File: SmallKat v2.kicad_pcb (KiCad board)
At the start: 2 copper layers, 89 x 99 mm, 187 parts, among them IC1 TPS562201DDCR, IC2 TPS40192DRCT, J1 Conn_01x03_Male, J10 Conn_01x03_Male, J11 Conn_01x03_Male, J12 Conn_01x03_Male, J13 Conn_01x03_Male, J14 Conn_01x03_Male, J15 Conn_01x03_Male, J16 Conn_01x03_Male, J17 Conn_01x03_Male, J18 Conn_01x02_Male, J19 USB_C_Receptacle, J2 Conn_01x03_Male, J20 USB_C_Receptacle, J3 Conn_01x03_Male, J4 Conn_01x03_Male, J5 Conn_01x03_Male, J6 Conn_01x03_Male, J7 Conn_01x03_Male, J8 Conn_01x03_Male, J9 Conn_01x02_Male, Q1 BUK9M120-100EX, Q2 BUK9M120-100EX, Q3 MMBT3904, Q4 MMBT3904, Q5 MMBT3904, Q6 MMBT3904, Q7 2N3905, SW1 SW_SPST, SW2 SW_SPST, SW3 SW_SPST, SW4 SW_SPST, U1 BNO055, U2 MIC5365-3.3YC5, U3 ESP32-WROOM-32, U4 CP2102N-A01-GQFN24, U5 MCP73831-2-OT, U6 MIC5365-3.3YC5, U7 ESP32-WROOM-32, U8 CP2102N-A01-GQFN24, U9 WIICHUCK, Y1 32.768kHz

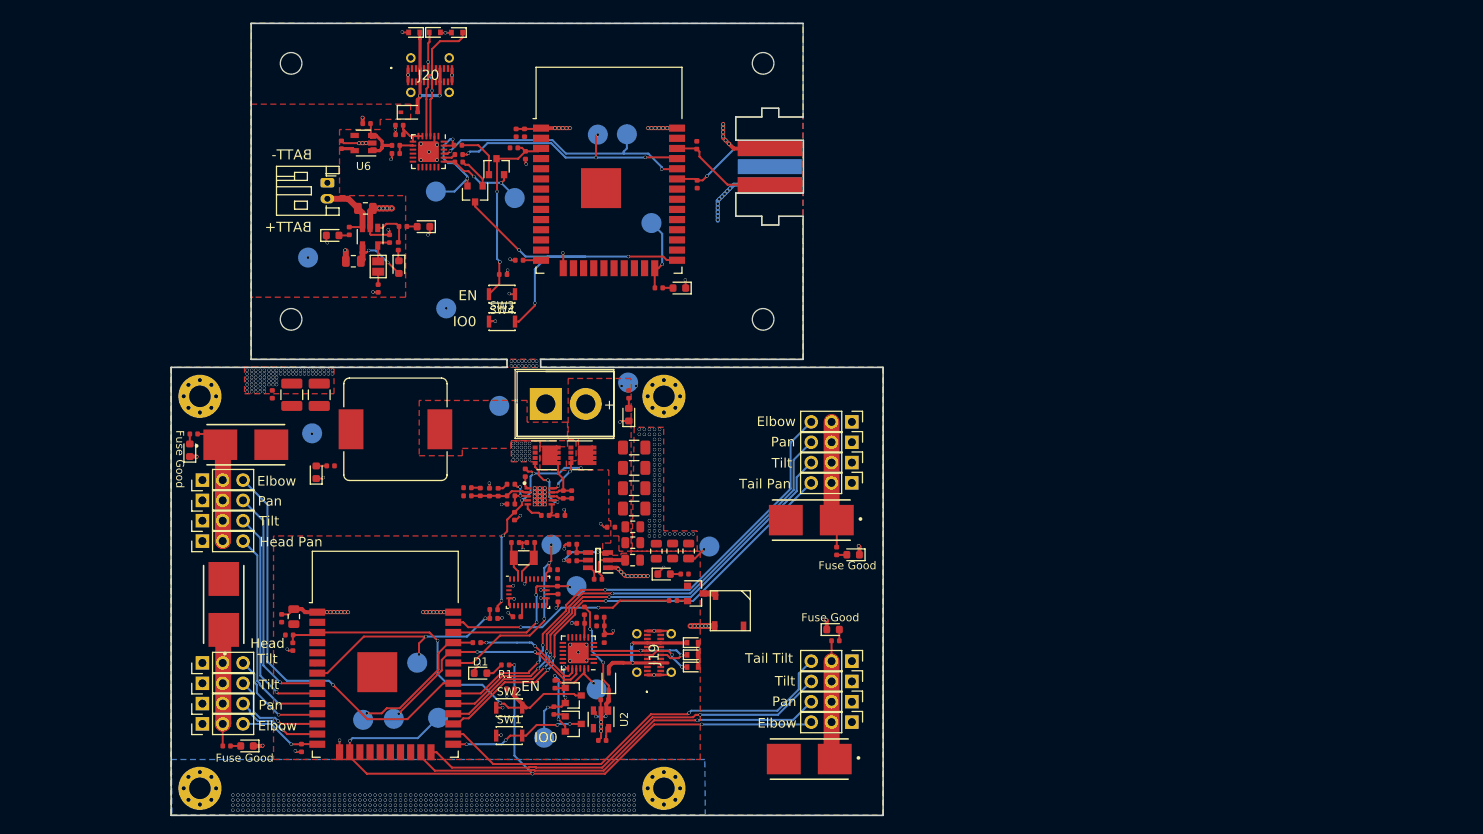
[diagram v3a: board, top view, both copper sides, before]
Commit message: In progress of charging implimentation
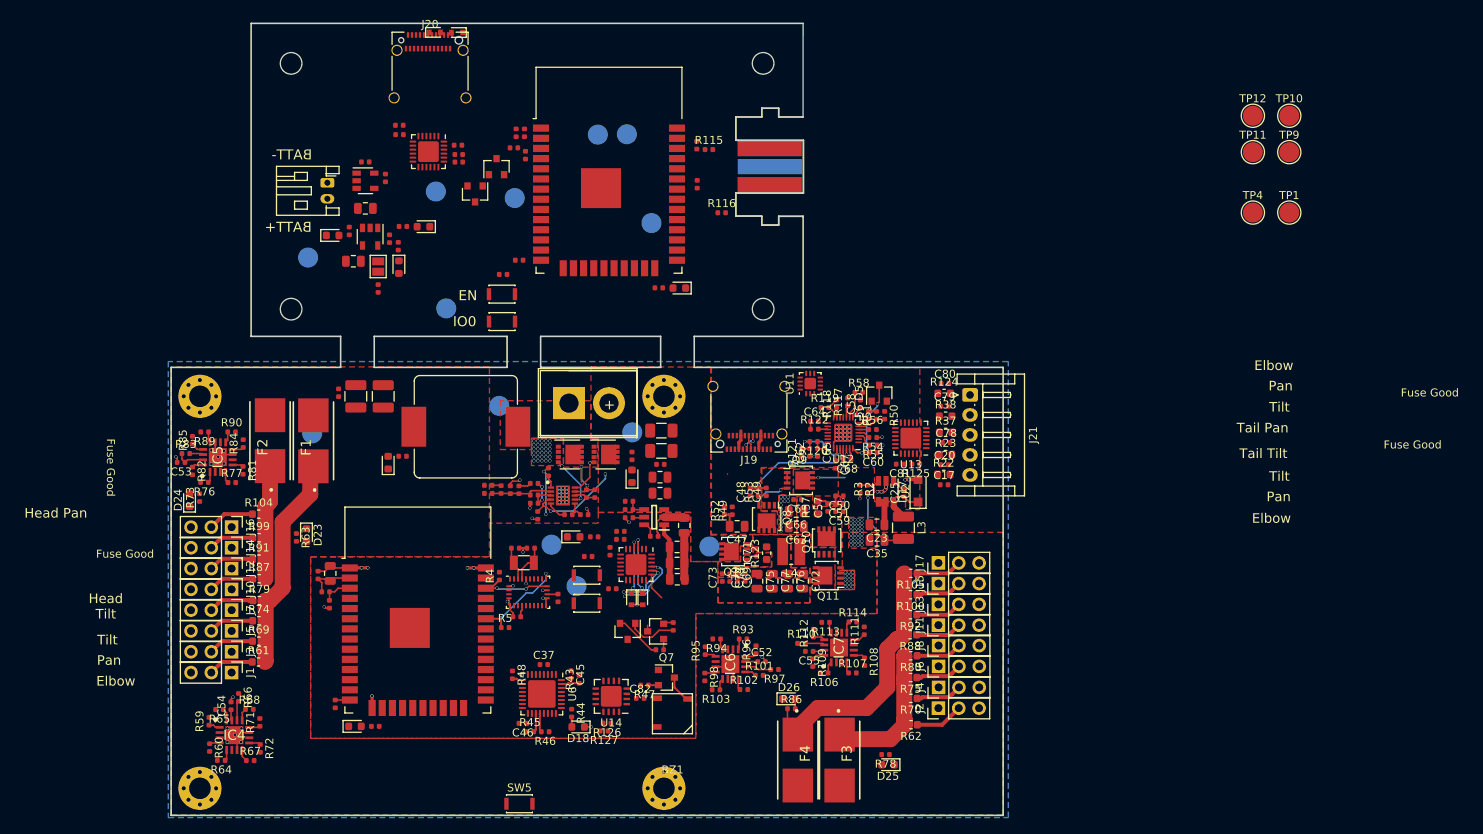
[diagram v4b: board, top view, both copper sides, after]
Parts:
- removed D13: D_TVS, Diode_SMD:D_SOD-523
- removed D14, D6: D_Schottky, Diode_SMD:D_SOD-323
- removed D19, D20: LED, LED_SMD:LED_0603_1608Metric
- added C30: 1uF, Capacitor_SMD:C_0402_1005Metric, F.Cu at (123.2, 61.2)
- added C42: 1uF, Capacitor_SMD:C_0402_1005Metric, F.Cu at (125.8, 63.2)
- added C45: 0.1uF, Capacitor_SMD:C_0402_1005Metric, F.Cu at (148.9, 125.3)
- added C46: 0.1uF, Capacitor_SMD:C_0402_1005Metric, F.Cu at (142.9, 131.4)
- added C47: 2.2uF, Capacitor_SMD:C_0805_2012Metric, F.Cu at (169.7, 106.8)
- added C48: 2200pF, Capacitor_SMD:C_0402_1005Metric, F.Cu at (171.3, 102.5)
- added C49: 0.1uF, Capacitor_SMD:C_0402_1005Metric, F.Cu at (173.3, 102.4)
- added C50: 1uF, Capacitor_SMD:C_0402_1005Metric, F.Cu at (182.5, 103.0)
- added C51: 0.1uF, Capacitor_SMD:C_0402_1005Metric, F.Cu at (182.5, 104.0)
- added C52: 0.1uF, Capacitor_SMD:C_0402_1005Metric, F.Cu at (172.8, 123.7)
- added C53: 0.1uF, Capacitor_SMD:C_0402_1005Metric, F.Cu at (100.2, 98.8)
- added C54: 0.1uF, Capacitor_SMD:C_0402_1005Metric, F.Cu at (106.5, 129.2)
- added C55: 0.1uF, Capacitor_SMD:C_0402_1005Metric, F.Cu at (178.7, 122.4)
- added C56: 100pF, Capacitor_SMD:C_0402_1005Metric, F.Cu at (186.1, 92.8)
- added C57: 0.1uF, Capacitor_SMD:C_0402_1005Metric, F.Cu at (181.1, 104.4)
- added C58: 100pF, Capacitor_SMD:C_0402_1005Metric, F.Cu at (185.1, 91.5)
- added C59: 0.1uF, Capacitor_SMD:C_0402_1005Metric, F.Cu at (182.5, 104.9)
- added C60: 1uF, Capacitor_SMD:C_0402_1005Metric, F.Cu at (186.7, 97.5)
- added C61: 1uF, Capacitor_SMD:C_0402_1005Metric, F.Cu at (177.2, 103.4)
- added C62: 0.01uF, Capacitor_SMD:C_0402_1005Metric, F.Cu at (178.8, 97.5)
- added C63: 10uF, Capacitor_SMD:C_0805_2012Metric, F.Cu at (177.1, 106.8)
- added C64: 0.1uF, Capacitor_SMD:C_0402_1005Metric, F.Cu at (179.4, 93.6)
- added C65: 1uF, Capacitor_SMD:C_0402_1005Metric, F.Cu at (179.8, 97.5)
- added C66: 10uF, Capacitor_SMD:C_0805_2012Metric, F.Cu at (177.1, 104.9)
- added C67: 470pF, Capacitor_SMD:C_0402_1005Metric, F.Cu at (182.0, 99.0)
- added C68: 0.047uF, Capacitor_SMD:C_0402_1005Metric, F.Cu at (183.5, 98.4)
- added C69: 10uF, Capacitor_SMD:C_0402_1005Metric, F.Cu at (169.8, 113.2)
- added C70: 0.1uF, Capacitor_SMD:C_0402_1005Metric, F.Cu at (170.7, 113.1)
- added C71: 0.1uF, Capacitor_SMD:C_0402_1005Metric, F.Cu at (172.2, 110.0)
- added C72: 22uF, Capacitor_SMD:C_0805_2012Metric, F.Cu at (177.9, 113.6)
- added C73: 0.1uF, Capacitor_SMD:C_0402_1005Metric, F.Cu at (167.8, 113.2)
- added C74: 10uF, Capacitor_SMD:C_0402_1005Metric, F.Cu at (168.8, 113.2)
- added C75: 22uF, Capacitor_SMD:C_0805_2012Metric, F.Cu at (172.2, 113.6)
- added C76: 22uF, Capacitor_SMD:C_0805_2012Metric, F.Cu at (176.0, 113.6)
- added C77: 22uF, Capacitor_SMD:C_0805_2012Metric, F.Cu at (174.1, 113.6)
- added C78: 0.1uF, Capacitor_SMD:C_0402_1005Metric, F.Cu at (195.8, 96.3)
- added C79: 0.1uF, Capacitor_SMD:C_0402_1005Metric, F.Cu at (195.7, 91.7)
- added C80: 0.1uF, Capacitor_SMD:C_0402_1005Metric, F.Cu at (195.7, 88.9)
- added C81: 1uF, Capacitor_SMD:C_0402_1005Metric, F.Cu at (190.1, 99.0)
- added C82: 1uF, Capacitor_SMD:C_0402_1005Metric, F.Cu at (157.6, 128.2)
- added D23: LED, LED_SMD:LED_0603_1608Metric, F.Cu at (115.9, 107.8)
- added D24: LED, LED_SMD:LED_0603_1608Metric, F.Cu at (101.3, 103.5)
- added D25: LED, LED_SMD:LED_0603_1608Metric, F.Cu at (188.6, 136.5)
- added D26: LED, LED_SMD:LED_0603_1608Metric, F.Cu at (176.2, 128.3)
- added IC4: MAX34409ETE+, MAX34409ETE+:QFN65P400X400X80-17N, F.Cu at (106.9, 132.8)
- added IC5: MAX34409ETE+, MAX34409ETE+:QFN65P400X400X80-17N, F.Cu at (104.8, 98.1)
- added IC6: MAX34409ETE+, MAX34409ETE+:QFN65P400X400X80-17N, F.Cu at (168.9, 124.0)
- added IC7: MAX34409ETE+, MAX34409ETE+:QFN65P400X400X80-17N, F.Cu at (182.4, 121.9)
- added J21: Conn_01x05_Male, Connector_JST:JST_EH_S5B-EH_1x05_P2.50mm_Horizontal, F.Cu at (198.8, 90.3)
- added L3: 15uH, Inductor_SMD:L_1210_3225Metric, F.Cu at (190.5, 106.9)
- added L4: L, Inductor_SMD:L_Wuerth_MAPI-3020, F.Cu at (176.5, 109.9)
- added Q10: CSD17307Q5A, Package_TO_SOT_SMD:LFPAK33, F.Cu at (180.9, 108.7)
- added Q11: CSD17307Q5A, Package_TO_SOT_SMD:LFPAK33, F.Cu at (181.1, 112.9)
- added Q12: Si7141DP, Package_TO_SOT_SMD:LFPAK33, F.Cu at (169.4, 109.9)
- added Q8: BUK9M120-100EX, Package_TO_SOT_SMD:LFPAK33, F.Cu at (173.4, 105.7)
- added Q9: BUK9M120-100EX, Package_TO_SOT_SMD:LFPAK33, F.Cu at (177.5, 101.0)
- added R100: 0.01R, Resistor_SMD:R_0603_1608Metric, F.Cu at (191.4, 115.3)
- added R101: 100R, Resistor_SMD:R_0402_1005Metric, F.Cu at (172.5, 125.4)
- added R102: 100R, Resistor_SMD:R_0402_1005Metric, F.Cu at (170.6, 127.2)
- added R103: 100R, Resistor_SMD:R_0402_1005Metric, F.Cu at (167.1, 127.2)
- added R104: 0.01R, Resistor_SMD:R_0603_1608Metric, F.Cu at (109.9, 105.2)
- added R105: 0.01R, Resistor_SMD:R_0603_1608Metric, F.Cu at (191.4, 112.6)
- added R106: 100R, Resistor_SMD:R_0402_1005Metric, F.Cu at (180.6, 125.1)
- added R107: 100R, Resistor_SMD:R_0402_1005Metric, F.Cu at (184.1, 125.1)
- added R108: 100R, Resistor_SMD:R_0402_1005Metric, F.Cu at (185.7, 123.7)
- added R109: 100R, Resistor_SMD:R_0402_1005Metric, F.Cu at (179.2, 123.8)
- added R110: 0R, Resistor_SMD:R_0402_1005Metric, F.Cu at (177.8, 121.4)
- added R111: 100R, Resistor_SMD:R_0402_1005Metric, F.Cu at (185.6, 119.8)
- added R112: 100R, Resistor_SMD:R_0402_1005Metric, F.Cu at (179.2, 120.1)
- added R113: 100R, Resistor_SMD:R_0402_1005Metric, F.Cu at (180.8, 118.8)
- added R114: 100R, Resistor_SMD:R_0402_1005Metric, F.Cu at (184.2, 118.7)
- added R115: 10K, Resistor_SMD:R_0402_1005Metric, F.Cu at (166.2, 59.6)
- added R116: 10K, Resistor_SMD:R_0402_1005Metric, F.Cu at (167.8, 67.5)
- added R117: 10K, Resistor_SMD:R_0402_1005Metric, F.Cu at (183.5, 91.2)
- added R118: 3M, Resistor_SMD:R_0402_1005Metric, F.Cu at (182.1, 91.5)
- added R119: 10K, Resistor_SMD:R_0402_1005Metric, F.Cu at (180.7, 91.9)
- added R120: 316K, Resistor_SMD:R_0402_1005Metric, F.Cu at (179.3, 96.2)
- added R121: 100K, Resistor_SMD:R_0402_1005Metric, F.Cu at (177.8, 97.5)
- added R122: 10R, Resistor_SMD:R_0402_1005Metric, F.Cu at (179.4, 94.6)
- added R123: 0.01R, Resistor_SMD:R_0603_1608Metric, F.Cu at (173.4, 110.1)
- added R124: 47R, Resistor_SMD:R_0603_1608Metric, F.Cu at (195.6, 90.1)
- added R125: 10K, Resistor_SMD:R_0402_1005Metric, F.Cu at (192.1, 99.0)
- added R126: 10K, Resistor_SMD:R_0402_1005Metric, F.Cu at (153.4, 131.3)
- added R127: 10K, Resistor_SMD:R_0402_1005Metric, F.Cu at (153.1, 132.3)
- added R48: 10K, Resistor_SMD:R_0402_1005Metric, F.Cu at (141.6, 125.3)
- added R49: 3.9K, Resistor_SMD:R_0402_1005Metric, F.Cu at (169.1, 104.8)
- added R50: 430K, Resistor_SMD:R_0402_1005Metric, F.Cu at (188.2, 92.9)
- added R51: 66.5K, Resistor_SMD:R_0402_1005Metric, F.Cu at (187.1, 92.9)
- added R52: 3.9K, Resistor_SMD:R_0402_1005Metric, F.Cu at (168.2, 104.8)
- added R53: 4.7R, Resistor_SMD:R_0402_1005Metric, F.Cu at (172.3, 102.5)
- added R54: 4.02K, Resistor_SMD:R_0402_1005Metric, F.Cu at (186.7, 95.7)
- added R55: 4.02K, Resistor_SMD:R_0402_1005Metric, F.Cu at (186.7, 96.6)
- added R56: 10K, Resistor_SMD:R_0402_1005Metric, F.Cu at (186.6, 94.7)
- added R57: 0.01R, Resistor_SMD:R_0603_1608Metric, F.Cu at (179.8, 104.4)
- added R58: 30.1K, Resistor_SMD:R_0402_1005Metric, F.Cu at (184.9, 90.0)
- added R59: 100R, Resistor_SMD:R_0402_1005Metric, F.Cu at (103.7, 131.1)
- added R60: 100R, Resistor_SMD:R_0402_1005Metric, F.Cu at (103.8, 134.4)
- added R61: 0.01R, Resistor_SMD:R_0603_1608Metric, F.Cu at (109.9, 123.7)
- added R62: 0.01R, Resistor_SMD:R_0603_1608Metric, F.Cu at (191.4, 131.6)
- added R63: 20K, Resistor_SMD:R_0402_1005Metric, F.Cu at (114.6, 108.1)
- added R64: 100R, Resistor_SMD:R_0402_1005Metric, F.Cu at (105.2, 136.0)
- added R65: 100R, Resistor_SMD:R_0402_1005Metric, F.Cu at (105.0, 129.7)
- added R66: 0R, Resistor_SMD:R_0402_1005Metric, F.Cu at (107.4, 128.1)
- added R67: 100R, Resistor_SMD:R_0402_1005Metric, F.Cu at (108.8, 136.0)
- added R68: 100R, Resistor_SMD:R_0402_1005Metric, F.Cu at (108.8, 129.6)
- added R69: 0.01R, Resistor_SMD:R_0603_1608Metric, F.Cu at (109.9, 121.1)
- added R70: 0.01R, Resistor_SMD:R_0603_1608Metric, F.Cu at (191.4, 128.2)
- added R71: 100R, Resistor_SMD:R_0402_1005Metric, F.Cu at (110.0, 131.2)
- added R72: 100R, Resistor_SMD:R_0402_1005Metric, F.Cu at (110.1, 134.5)
- added R73: 20K, Resistor_SMD:R_0402_1005Metric, F.Cu at (102.5, 103.2)
- added R74: 0.01R, Resistor_SMD:R_0603_1608Metric, F.Cu at (109.9, 118.5)
- added R75: 0.01R, Resistor_SMD:R_0603_1608Metric, F.Cu at (191.4, 125.7)
- added R76: 100R, Resistor_SMD:R_0402_1005Metric, F.Cu at (103.1, 101.2)
- added R77: 100R, Resistor_SMD:R_0402_1005Metric, F.Cu at (106.5, 101.3)
- added R78: 20K, Resistor_SMD:R_0402_1005Metric, F.Cu at (188.3, 135.3)
- added R79: 0.01R, Resistor_SMD:R_0603_1608Metric, F.Cu at (110.0, 116.0)
- added R80: 0.01R, Resistor_SMD:R_0603_1608Metric, F.Cu at (191.4, 122.9)
- added R81: 100R, Resistor_SMD:R_0402_1005Metric, F.Cu at (108.0, 99.8)
- added R82: 100R, Resistor_SMD:R_0402_1005Metric, F.Cu at (101.6, 99.8)
- added R83: 0R, Resistor_SMD:R_0402_1005Metric, F.Cu at (100.8, 97.7)
- added R84: 100R, Resistor_SMD:R_0402_1005Metric, F.Cu at (108.0, 96.4)
- added R85: 100R, Resistor_SMD:R_0402_1005Metric, F.Cu at (101.6, 96.0)
- added R86: 20K, Resistor_SMD:R_0402_1005Metric, F.Cu at (176.5, 129.6)
- added R87: 0.01R, Resistor_SMD:R_0603_1608Metric, F.Cu at (110.0, 113.3)
- added R88: 0.01R, Resistor_SMD:R_0603_1608Metric, F.Cu at (191.3, 120.3)
- added R89: 100R, Resistor_SMD:R_0402_1005Metric, F.Cu at (103.2, 95.0)
- added R90: 100R, Resistor_SMD:R_0402_1005Metric, F.Cu at (106.5, 95.0)
- added R91: 0.01R, Resistor_SMD:R_0603_1608Metric, F.Cu at (109.9, 110.8)
- added R92: 0.01R, Resistor_SMD:R_0603_1608Metric, F.Cu at (191.4, 117.8)
- added R93: 100R, Resistor_SMD:R_0402_1005Metric, F.Cu at (170.4, 120.8)
- added R94: 100R, Resistor_SMD:R_0402_1005Metric, F.Cu at (167.2, 120.8)
- added R95: 100R, Resistor_SMD:R_0402_1005Metric, F.Cu at (165.7, 122.3)
- added R96: 100R, Resistor_SMD:R_0402_1005Metric, F.Cu at (172.1, 122.2)
- added R97: 0R, Resistor_SMD:R_0402_1005Metric, F.Cu at (174.4, 124.7)
- added R98: 100R, Resistor_SMD:R_0402_1005Metric, F.Cu at (165.7, 125.6)
- added R99: 0.01R, Resistor_SMD:R_0603_1608Metric, F.Cu at (110.0, 108.2)
- added SW5: SW_SPST, Button_Switch_SMD:SW_SPST_CK_KXT3, F.Cu at (142.5, 141.4)
- added U10: MIC5365-3.3YC5, Package_TO_SOT_SMD:SOT-23-5, F.Cu at (123.3, 63.6)
- added U11: FUSB302BMPX, Package_DFN_QFN:WQFN-14-1EP_2.5x2.5mm_P0.5mm_EP1.45x1.45mm, F.Cu at (178.8, 88.9)
- added U12: BQ24770, Package_DFN_QFN:QFN-28-1EP_4x4mm_P0.4mm_EP2.3x2.3mm, F.Cu at (183.0, 95.0)
- added U13: bq76925, Package_DFN_QFN:QFN-24-1EP_4x4mm_P0.5mm_EP2.6x2.6mm, F.Cu at (191.4, 95.7)
- added U14: PCA9641, Package_DFN_QFN:UQFN-16-1EP_4x4mm_P0.65mm_EP2.6x2.6mm, F.Cu at (154.0, 128.0)
- C17, C20: value 47uF -> 0.1uF; footprint Capacitor_SMD:C_1206_3216Metric -> Capacitor_SMD:C_0402_1005Metric
- C23: value 1uF -> 2.2uF; footprint Capacitor_SMD:C_0402_1005Metric -> Capacitor_SMD:C_0805_2012Metric
- C25, C37: value 1uF -> 0.1uF
- C35: value 1uF -> 10uF; footprint Capacitor_SMD:C_0402_1005Metric -> Capacitor_SMD:C_0805_2012Metric
- D17: value LED -> MA2YD26; footprint LED_SMD:LED_0603_1608Metric -> Diode_SMD:D_SOD-123F
- D5: value D_TVS -> BAT54C; footprint Diode_SMD:D_SOD-523 -> Package_TO_SOT_SMD:SOT-23
- J19, J20: footprint U263-241N-4BQC11-1:U263241N4BQC111 -> Connector_USB:USB_C_Receptacle_Amphenol_12401610E4-2A_CircularHoles
- R1, R44: value R -> 330R
- R2: value 10K -> 1K
- R20: value 1K -> 20K
- R22, R37: value 10K -> 47R; footprint Resistor_SMD:R_0402_1005Metric -> Resistor_SMD:R_0603_1608Metric
- R23, R38: value 20K -> 47R; footprint Resistor_SMD:R_0402_1005Metric -> Resistor_SMD:R_0603_1608Metric
- R3: value 6.2k -> 3.4K
- R45, R46, R47: value R -> 10K
- R6: value 4.7K -> 120K
- TP1, TP10, TP11, TP12, TP4, TP9: moved to F.Cu
- U2: value MIC5365-3.3YC5 -> LM2840Y; footprint Package_TO_SOT_SMD:SOT-23-5 -> Package_TO_SOT_SMD:TSOT-23-6
- U6: value MIC5365-3.3YC5 -> STM32L432KBUx; footprint Package_TO_SOT_SMD:SOT-23-5 -> Package_DFN_QFN:QFN-32-1EP_5x5mm_P0.5mm_EP3.45x3.45mm
- moved TP9 135.8 mm to (238.7, 60.0)
- moved TP10 135.0 mm to (238.7, 55.4)
- moved TP1 123.7 mm to (238.7, 67.5)
- moved TP4 118.7 mm to (234.2, 67.5)
- moved TP12 117.9 mm to (234.2, 55.4)
- moved TP11 106.0 mm to (234.2, 60.0)
- moved J8 94.3 mm to (194.9, 121.7)
- moved J6 93.8 mm to (194.9, 124.2)
- moved J4 92.1 mm to (194.9, 126.9)
- moved J2 92.0 mm to (194.9, 129.5)
- moved D17 89.7 mm to (192.3, 102.3), turned to 90 degrees
- moved C35 82.4 mm to (187.2, 108.5)
- moved J10 79.3 mm to (106.5, 114.6)
- moved J12 78.8 mm to (106.5, 112.0)
- moved J16 78.3 mm to (106.5, 106.8)
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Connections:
- C17 pad 1: +BATT -> Net-(C17-Pad1)
- C20 pad 1: +BATT -> Net-(C20-Pad1)
- C23 pad 1: +5V -> VBUS
- C25 pad 1: +3V3 -> Net-(C25-Pad1)
- C25 pad 2: GND -> Net-(C25-Pad2)
- C35 pad 1: +5V -> Net-(C35-Pad1)
- D17 pad 1: GND -> Net-(C25-Pad1)
- D17 pad 2: Net-(D17-Pad2) -> GND
- D5 pad 1: Net-(D5-Pad1) -> +BATT
- D5 pad 2: GND -> VBUS
- F1 pad 1: Net-(F1-Pad1) -> /MainBoard/Servos/6V1
- F2 pad 1: Net-(F2-Pad1) -> /MainBoard/Servos/6V2
- F3 pad 1: Net-(F3-Pad1) -> /MainBoard/Servos/6V3
- F4 pad 1: Net-(F4-Pad1) -> /MainBoard/Servos/6V4
- H3 pad 1: Net-(H3-Pad1) -> +BATT
- J1 pad 1: GND -> /MainBoard/SERVO0
- J1 pad 2: Net-(F1-Pad1) -> /MainBoard/Servos/S1
- J1 pad 3: /MainBoard/SERVO0 -> GND
- J10 pad 1: GND -> /MainBoard/SERVO4
- J10 pad 2: Net-(F3-Pad1) -> /MainBoard/Servos/S5
- J10 pad 3: /MainBoard/SERVO8 -> GND
- J11 pad 1: GND -> /MainBoard/SERVO12
- J11 pad 2: Net-(F3-Pad1) -> /MainBoard/Servos/S13
- J11 pad 3: /MainBoard/SERVO9 -> GND
- J12 pad 1: GND -> /MainBoard/SERVO5
- J12 pad 2: Net-(F3-Pad1) -> /MainBoard/Servos/S6
- J12 pad 3: /MainBoard/SERVO10 -> GND
- J13 pad 1: GND -> /MainBoard/SERVO13
- J13 pad 2: Net-(F3-Pad1) -> /MainBoard/Servos/S14
- J13 pad 3: /MainBoard/SERVO11 -> GND
- J14 pad 1: GND -> /MainBoard/SERVO6
- J14 pad 2: Net-(F4-Pad1) -> /MainBoard/Servos/S7
- J14 pad 3: /MainBoard/SERVO12 -> GND
- J15 pad 1: GND -> /MainBoard/SERVO14
- J15 pad 2: Net-(F4-Pad1) -> /MainBoard/Servos/S15
- J15 pad 3: /MainBoard/SERVO13 -> GND
- J16 pad 1: GND -> /MainBoard/SERVO7
- J16 pad 2: Net-(F4-Pad1) -> /MainBoard/Servos/S8
- J16 pad 3: /MainBoard/SERVO14 -> GND
- J17 pad 1: GND -> /MainBoard/SERVO15
- J17 pad 2: Net-(F4-Pad1) -> /MainBoard/Servos/S16
- J17 pad 3: /MainBoard/SERVO15 -> GND
- J19 pad A4: Net-(D5-Pad1) -> VBUS
- J19 pad A5: (no net) -> /MainBoard/CC1
- J19 pad A9: Net-(D5-Pad1) -> VBUS
- J19 pad B4: Net-(D5-Pad1) -> VBUS
- J19 pad B5: (no net) -> /MainBoard/CC2
- J19 pad B9: Net-(D5-Pad1) -> VBUS
- J2 pad 1: GND -> /MainBoard/SERVO8
- J2 pad 2: Net-(F1-Pad1) -> /MainBoard/Servos/S9
- J2 pad 3: /MainBoard/SERVO1 -> GND
- J20 pad A4: Net-(D13-Pad1) -> VBUS
- J20 pad A9: Net-(D13-Pad1) -> VBUS
- J20 pad B4: Net-(D13-Pad1) -> VBUS
- J20 pad B9: Net-(D13-Pad1) -> VBUS
- J3 pad 1: GND -> /MainBoard/SERVO1
- J3 pad 2: Net-(F1-Pad1) -> /MainBoard/Servos/S2
- J3 pad 3: /MainBoard/SERVO2 -> GND
- J4 pad 1: GND -> /MainBoard/SERVO9
- J4 pad 2: Net-(F1-Pad1) -> /MainBoard/Servos/S10
- J4 pad 3: /MainBoard/SERVO3 -> GND
- J5 pad 1: GND -> /MainBoard/SERVO2
- J5 pad 2: Net-(F2-Pad1) -> /MainBoard/Servos/S3
- J5 pad 3: /MainBoard/SERVO4 -> GND
- J6 pad 1: GND -> /MainBoard/SERVO10
- J6 pad 2: Net-(F2-Pad1) -> /MainBoard/Servos/S11
- J6 pad 3: /MainBoard/SERVO5 -> GND
- J7 pad 1: GND -> /MainBoard/SERVO3
- J7 pad 2: Net-(F2-Pad1) -> /MainBoard/Servos/S4
- J7 pad 3: /MainBoard/SERVO6 -> GND
- J8 pad 1: GND -> /MainBoard/SERVO11
- J8 pad 2: Net-(F2-Pad1) -> /MainBoard/Servos/S12
- J8 pad 3: /MainBoard/SERVO7 -> GND
- R10 pad 1: +BATT -> /MainBoard/3.3VEN
- R17 pad 1: +BATT -> /MainBoard/6VEN
- R2 pad 1: /MainBoard/BATTMONITOR -> Net-(R2-Pad1)
- R22 pad 1: Net-(R22-Pad1) -> Net-(C17-Pad1)
- R22 pad 2: +5V -> /MainBoard/BatteryBalancer/C4
- R23 pad 1: GND -> Net-(C20-Pad1)
- R23 pad 2: Net-(R22-Pad1) -> /MainBoard/BatteryBalancer/C3
- R3 pad 1: +BATT -> Net-(C35-Pad1)
- R3 pad 2: /MainBoard/BATTMONITOR -> Net-(R2-Pad1)
- R37 pad 1: Net-(R37-Pad1) -> Net-(C78-Pad1)
- R37 pad 2: +5V -> /MainBoard/BatteryBalancer/C2
- R38 pad 1: GND -> Net-(C79-Pad1)
- R38 pad 2: Net-(R37-Pad1) -> /MainBoard/BatteryBalancer/C1
- R43 pad 1: Net-(Q7-Pad2) -> Net-(R43-Pad1)
- R43 pad 2: /MainBoard/BUZZER -> +3V3
- R44 pad 1: Net-(F1-Pad1) -> /MainBoard/SafetyMCU/MONITORING
- R44 pad 2: Net-(D17-Pad2) -> Net-(D18-Pad2)
- R45 pad 1: Net-(F2-Pad1) -> +3V3
- R45 pad 2: Net-(D18-Pad2) -> /MainBoard/SAFETYSCL
- R46 pad 1: Net-(F3-Pad1) -> +3V3
- R46 pad 2: Net-(D19-Pad2) -> /MainBoard/SAFETYSDA
- R47 pad 1: Net-(F4-Pad1) -> Net-(Q7-Pad2)
- R47 pad 2: Net-(D20-Pad2) -> /MainBoard/SafetyMCU/BUZZER
- TP4 pad 1: /MainBoard/BATTMONITOR -> (no net)
- U2 pad 1: +5V -> Net-(C25-Pad2)
- U2 pad 3: +5V -> Net-(R2-Pad1)
- U2 pad 4: (no net) -> VBUS
- U2 pad 5: +3V3 -> VBUS
- U3 pad 37: /MainBoard/BUZZER -> (no net)
- U3 pad 7: /MainBoard/BATTMONITOR -> (no net)
- U4 pad 8: Net-(R22-Pad1) -> +3V3
- U6 pad 1: +5V -> +3V3
- U6 pad 2: GND -> (no net)
- U6 pad 3: +5V -> (no net)
- U8 pad 8: Net-(R37-Pad1) -> +3V3
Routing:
- net /MainBoard/SERVO8: track 90.6 -> 0.00 mm, vias 4 -> 0
- net /MainBoard/SERVO15: track 64.5 -> 0.00 mm, vias 3 -> 0
- net GND: track 125.7 -> 61.5 mm, vias 315 -> 170
- net /MainBoard/SERVO14: track 62.8 -> 0.00 mm, vias 3 -> 0
- net /MainBoard/SERVO13: track 61.1 -> 0.00 mm, vias 3 -> 0
- net /MainBoard/SERVO12: track 59.7 -> 0.00 mm, vias 3 -> 0
- net /MainBoard/SERVO9: track 53.7 -> 0.00 mm, vias 1 -> 0
- net /MainBoard/SERVO10: track 52.8 -> 0.00 mm, vias 1 -> 0
- net /MainBoard/SERVO11: track 52.8 -> 0.00 mm, vias 1 -> 0
- net /MainBoard/SERVO7: track 52.0 -> 0.00 mm, vias 1 -> 0
- net /ControllerBoard/ESP32Module_CONTROLLER/IO0: track 43.5 -> 0.00 mm, vias 3 -> 0
- net /MainBoard/ESP32Module/EN: track 47.2 -> 3.79 mm, vias 2 -> 0
- net /ControllerBoard/ESP32Module_CONTROLLER/RXD: track 34.1 -> 0.00 mm, vias 2 -> 0
- net /MainBoard/Servos/6V4: track 0.00 -> 33.2 mm
- net +5V: track 32.5 -> 0.00 mm, vias 7 -> 0
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- added copper zone on F.Cu, net /MainBoard/Sheet5DD4BDB8/PHASE
- added copper zone on F.Cu, net /MainBoard/Sheet5DD4BDB8/SRN
- added copper zone on F.Cu, net /MainBoard/Sheet5DD4BDB8/SRP
- added copper zone on In1.Cu, net GND
- added copper zone on In2.Cu, net GND
- added copper zone on F.Cu, net Net-(C49-Pad1)
- added copper zone on F.Cu, net Net-(C50-Pad2)
- added copper zone on F.Cu, net Net-(C57-Pad1)
- added copper zone on F.Cu, net Net-(U6-Pad25)
- added copper zone on F.Cu, net VBUS
- removed copper zone on F.Cu, net +3V3
- removed copper zone on F.Cu, net +5V
- removed copper zone on B.Cu, net +6V
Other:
- board size 89 x 99 mm -> 104 x 99 mm
- copper layers 2 -> 4
- board text added: "Rev 1.1"
- board text removed: "BATT IN"
- board text removed: "IO19"
- board text removed: "Rev 1.0"

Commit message: Routing done
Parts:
- removed C30, C42: 1uF, Capacitor_SMD:C_0402_1005Metric
- removed C33, C34: 10uF, Capacitor_SMD:C_0805_2012Metric
- removed C36: 22uF, Capacitor_SMD:C_0805_2012Metric
- removed C38, C40, C41, C43, C44: 0.1uF, Capacitor_SMD:C_0402_1005Metric
- removed C39: 4.7uF, Capacitor_SMD:C_0402_1005Metric
- removed D10, D11, D12, D9: LED, LED_SMD:LED_0603_1608Metric
- removed D15, D16: D_TVS, Diode_SMD:D_SOD-523
- removed H5, H6, H7, H8: MountingHole, MountingHole:MountingHole_2.7mm_M2.5
- removed J18: Conn_01x02_Male, Connector_JST:JST_PH_S2B-PH-K_1x02_P2.00mm_Horizontal
- removed J20: USB_C_Receptacle, Connector_USB:USB_C_Receptacle_Amphenol_12401610E4-2A_CircularHoles
- removed JP1: Jumper_NO_Small, Jumper:SolderJumper-2_P1.3mm_Open_Pad1.0x1.5mm
- removed Q5, Q6: MMBT3904, Package_TO_SOT_SMD:SOT-23
- removed R115, R116, R29, R30, R32, R36, R40, R41, R42: 10K, Resistor_SMD:R_0402_1005Metric
- removed R28, R31: 330R, Resistor_SMD:R_0402_1005Metric
- removed R33: 2.5K, Resistor_SMD:R_0402_1005Metric
- removed R34, R35, R39: 470R, Resistor_SMD:R_0402_1005Metric
- removed SW3, SW4: SW_SPST, Button_Switch_SMD:SW_SPST_CK_KXT3
- removed TP13, TP14, TP15, TP16, TP17, TP18, TP19, TP4: TestPoint, TestPoint:TestPoint_Pad_D2.5mm
- removed U10: MIC5365-3.3YC5, Package_TO_SOT_SMD:SOT-23-5
- removed U5: MCP73831-2-OT, Package_TO_SOT_SMD:SOT-23-5
- removed U7: ESP32-WROOM-32, RF_Module:ESP32-WROOM-32
- removed U8: CP2102N-A01-GQFN24, Package_DFN_QFN:QFN-24-1EP_4x4mm_P0.5mm_EP2.6x2.6mm
- removed U9: WIICHUCK, WIICHUCK:CHUCK
- added TP20: TestPoint, TestPoint:TestPoint_Pad_D1.5mm, B.Cu at (146.7, 135.3)
- added TP21: TestPoint, TestPoint:TestPoint_Pad_D1.5mm, B.Cu at (149.0, 134.2)
- added TP22: TestPoint, TestPoint:TestPoint_Pad_D1.5mm, B.Cu at (140.6, 131.8)
- added TP23: TestPoint, TestPoint:TestPoint_Pad_D1.5mm, B.Cu at (151.6, 134.0)
- TP1, TP10, TP11, TP12, TP9: footprint TestPoint:TestPoint_Pad_D2.5mm -> TestPoint:TestPoint_Pad_D1.5mm; moved to B.Cu
- TP2, TP3, TP5, TP6, TP7, TP8: footprint TestPoint:TestPoint_Pad_D2.5mm -> TestPoint:TestPoint_Pad_D1.5mm
- moved TP10 124.1 mm to (129.7, 114.6)
- moved TP9 117.6 mm to (134.7, 114.9)
- moved TP1 116.7 mm to (130.9, 112.1)
- moved TP12 100.5 mm to (154.6, 116.8)
- moved TP11 96.1 mm to (157.8, 118.2)
- moved D1 31.9 mm to (142.9, 107.8), turned to 180 degrees
- moved R1 28.8 mm to (140.4, 107.8), turned to 0 degrees
- moved TP8 16.0 mm to (130.9, 102.3)
- moved TP3 16.0 mm to (133.8, 112.2)
- moved TP2 15.6 mm to (133.9, 118.3)
- moved TP5 13.3 mm to (153.4, 105.8)
- moved R127 11.0 mm to (161.4, 125.2), turned to 0 degrees
- moved BZ1 9.84 mm to (153.6, 124.5), turned to 0 degrees
- moved R67 9.32 mm to (104.2, 128.0), turned to 180 degrees
- moved R126 9.22 mm to (161.1, 126.2), turned to 0 degrees
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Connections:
- C35 pad 1: Net-(C35-Pad1) -> +3.3VA
- C37 pad 1: +3V3 -> +3.3VA
- C45 pad 1: +3V3 -> +3.3VA
- C46 pad 1: +3V3 -> +3.3VA
- L3 pad 2: Net-(C35-Pad1) -> +3.3VA
- R1 pad 1: /MainBoard/SERVO8 -> /MainBoard/ESP32Module/IO23
- R101 pad 2: /MainBoard/Servos/S12 -> /MainBoard/Servos/S10
- R103 pad 2: /MainBoard/Servos/S11 -> /MainBoard/Servos/S9
- R112 pad 2: /MainBoard/Servos/S6 -> /MainBoard/Servos/S16
- R3 pad 1: Net-(C35-Pad1) -> +3.3VA
- R43 pad 2: +3V3 -> +3.3VA
- R45 pad 1: +3V3 -> +3.3VA
- R46 pad 1: +3V3 -> +3.3VA
- R48 pad 1: +3V3 -> +3.3VA
- R76 pad 2: /MainBoard/Servos/S5 -> /MainBoard/Servos/S6
- R81 pad 2: /MainBoard/Servos/S6 -> /MainBoard/Servos/S7
- R85 pad 2: /MainBoard/Servos/S8 -> /MainBoard/Servos/S5
- R90 pad 2: /MainBoard/Servos/S7 -> /MainBoard/Servos/S8
- R93 pad 2: /MainBoard/Servos/S9 -> /MainBoard/Servos/S12
- R95 pad 2: /MainBoard/Servos/S10 -> /MainBoard/Servos/S11
- TP1 pad 1: /MainBoard/SERVO8 -> /MainBoard/ESP32Module/IO23
- U14 pad 1: /MainBoard/SAFETYSCL -> /MainBoard/SCL
- U14 pad 16: /MainBoard/SAFETYSDA -> /MainBoard/SDA
- U14 pad 3: /MainBoard/SCL -> /MainBoard/SAFETYSCL
- U14 pad 4: /MainBoard/SDA -> /MainBoard/SAFETYSDA
- U3 pad 37: (no net) -> /MainBoard/ESP32Module/IO23
- U6 pad 1: +3V3 -> +3.3VA
- U6 pad 14: /MainBoard/SafetyMCU/MONITORING -> (no net)
- U6 pad 17: +3V3 -> +3.3VA
- U6 pad 22: (no net) -> /MainBoard/SafetyMCU/SOFTPOWER
- U6 pad 23: (no net) -> Net-(TP20-Pad1)
- U6 pad 24: (no net) -> Net-(TP21-Pad1)
- U6 pad 25: Net-(U6-Pad25) -> /MainBoard/SafetyMCU/MONITORING
- U6 pad 26: (no net) -> /MainBoard/SafetyMCU/BUZZER
- U6 pad 5: +3V3 -> +3.3VA
- U6 pad 6: /MainBoard/6VEN -> /MainBoard/3.3VEN
- U6 pad 7: /MainBoard/3.3VEN -> (no net)
- U6 pad 8: /MainBoard/SafetyMCU/BUZZER -> /MainBoard/6VEN
- U6 pad 9: /MainBoard/SafetyMCU/SOFTPOWER -> (no net)
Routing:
- net /MainBoard/_SCL: track 0.00 -> 131.4 mm, vias 0 -> 6
- net /MainBoard/_SDA: track 0.00 -> 128.6 mm, vias 0 -> 7
- net +3V3: track 19.9 -> 144.0 mm, vias 0 -> 254
- net /MainBoard/SAFETYSCL: track 2.39 -> 103.9 mm, vias 0 -> 9
- net /MainBoard/SAFETYSDA: track 2.37 -> 102.0 mm, vias 0 -> 10
- net /MainBoard/SERVO8: track 0.00 -> 80.0 mm, vias 0 -> 1
- net /MainBoard/Servos/6V4: track 33.2 -> 111.9 mm, vias 0 -> 104
- net /MainBoard/Servos/6V1: track 27.3 -> 104.9 mm, vias 0 -> 164
- net /MainBoard/Servos/6V3: track 17.8 -> 90.1 mm, vias 0 -> 71
- net /MainBoard/SERVO9: track 0.00 -> 69.2 mm, vias 0 -> 1
- net /MainBoard/SERVO10: track 0.00 -> 65.4 mm, vias 0 -> 1
- net /MainBoard/SERVO12: track 0.00 -> 62.2 mm, vias 0 -> 1
- net /MainBoard/SERVO15: track 0.00 -> 61.0 mm, vias 0 -> 1
- net +3.3VA: track 0.00 -> 60.7 mm, vias 0 -> 20
- net /MainBoard/SERVO14: track 0.00 -> 60.5 mm, vias 0 -> 1
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- added copper zone on F.Cu, net +3.3VA
- added copper zone on In1.Cu, net +3.3VA
- added copper zone on F.Cu, net +3V3
- added copper zone on In1.Cu, net +3V3
- added copper zone on In1.Cu, net +6V
- added copper zone on In1.Cu, net VBUS
- removed copper zone on F.Cu, net Net-(U6-Pad25)
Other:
- board size 104 x 99 mm -> 104 x 56 mm
- board text removed: "-"
- board text removed: "3.3v"
- board text removed: "5v"
- board text removed: "6v"
- board text removed: "BATT-"
- board text removed: "DTR"
- board text removed: "EN"
- board text removed: "GND"
- board text removed: "IO0"
- board text removed: "IO2"
- board text removed: "Keion Bisland"
- board text removed: "RTS"
- board text removed: "RX"
- board text removed: "Rev 1.1"
- board text removed: "SCL"
- board text removed: "SDA"
- board text removed: "SmallKat Mother Board"
- board text removed: "SmallKat Remote Controller Board"
- board text removed: "TX"
